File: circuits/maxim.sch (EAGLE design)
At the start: 5 parts, among them IC1 MAX662ACPA+

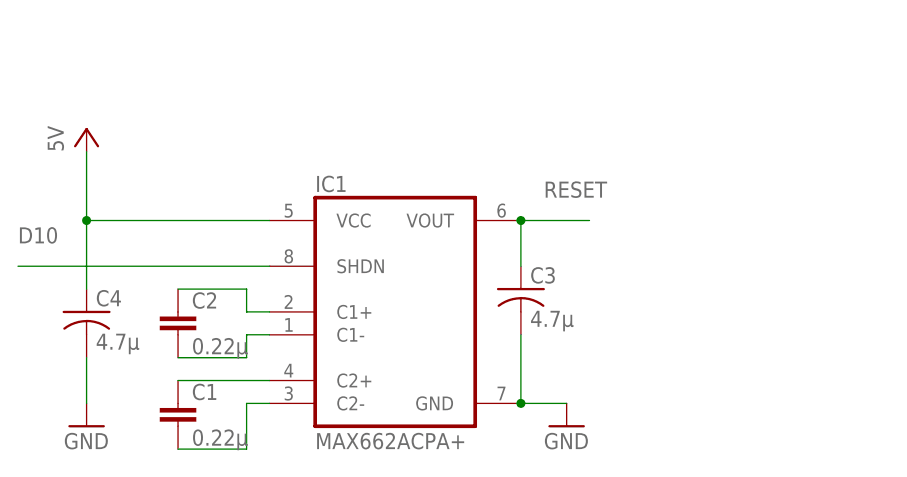
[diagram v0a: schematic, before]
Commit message: More documentation, started HVPP docs
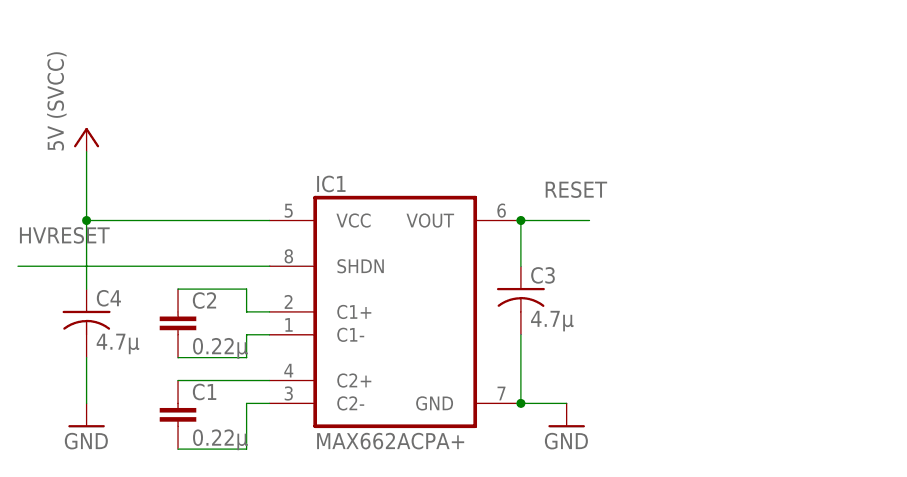
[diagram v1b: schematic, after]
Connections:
- net D10 renamed HVRESET
- net VCC renamed SVCC
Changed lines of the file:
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@@
 <part name="C2" library="rcl" deviceset="C-EU" device="025-024X044" value="0.22µ"/>
 <part name="GND1" library="supply1" deviceset="GND" device=""/>
-<part name="5V" library="supply1" deviceset="VCC" device="" value="5V"/>
+<part name="5V" library="supply1" deviceset="VCC" device="" value="5V (SVCC)"/>
 <part name="C3" library="rcl" deviceset="C-US" device="025-024X044" value="4.7µ"/>
 <part name="C4" library="rcl" deviceset="C-US" device="025-024X044" value="4.7µ"/>
@@
 </segment>
 </net>
-<net name="VCC" class="0">
+<net name="SVCC" class="0">
 <segment>
 <pinref part="IC1" gate="1" pin="VCC"/>
@@
 </segment>
 </net>
-<net name="D10" class="0">
+<net name="HVRESET" class="0">
 <segment>
 <pinref part="IC1" gate="1" pin="SHDN"/>

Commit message: Maxim circuit needs transistor anyway
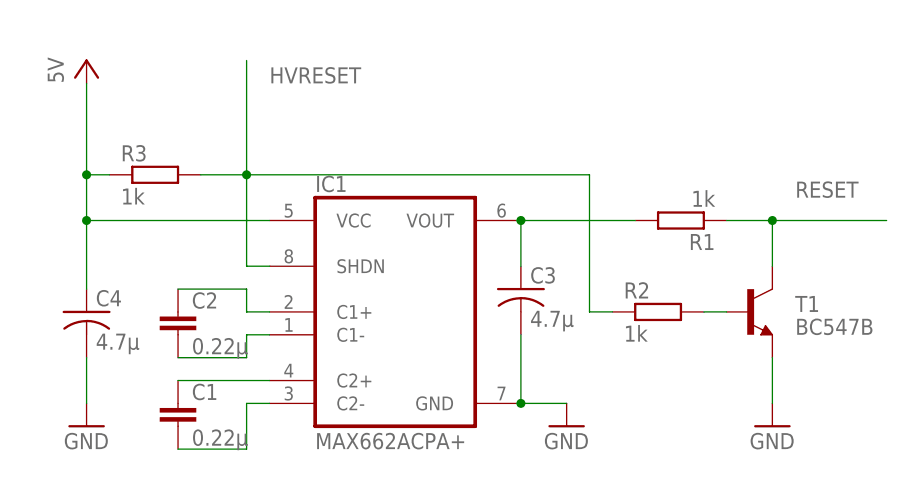
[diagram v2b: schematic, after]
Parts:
- added R1, R2, R3: 1k, eagle-ltspice:R
- added T1: BC547B, transistor:BC547
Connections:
- new net N$5: R2.2, T1.B
- new net VOUT: C3.1, IC1.VOUT, R1.2
- net GND: now also T1.E
- net HVRESET: now also R2.1, R3.2
- net RESET: now also R1.1, T1.C; no longer C3.1, IC1.VOUT
- net SVCC: now also R3.1
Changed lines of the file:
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@@
 <layer number="97" name="Info" color="7" fill="1" visible="yes" active="yes"/>
 <layer number="98" name="Guide" color="6" fill="1" visible="yes" active="yes"/>
+<layer number="99" name="SpiceOrder" color="5" fill="1" visible="yes" active="yes"/>
 </layers>
 <schematic xreflabel="%F%N/%S.%C%R" xrefpart="/%S.%C%R">
@@
 <part name="C2" library="rcl" deviceset="C-EU" device="025-024X044" value="0.22µ"/>
 <part name="GND1" library="supply1" deviceset="GND" device=""/>
-<part name="5V" library="supply1" deviceset="VCC" device="" value="5V (SVCC)"/>
+<part name="5V" library="supply1" deviceset="VCC" device="" value="5V"/>
 <part name="C3" library="rcl" deviceset="C-US" device="025-024X044" value="4.7µ"/>
 <part name="C4" library="rcl" deviceset="C-US" device="025-024X044" value="4.7µ"/>
 <part name="GND2" library="supply1" deviceset="GND" device=""/>
+<part name="T1" library="transistor" deviceset="BC547" device="" value="BC547B"/>
+<part name="GND3" library="supply1" deviceset="GND" device=""/>
+<part name="R1" library="eagle-ltspice" deviceset="R" device="" value="1k"/>
+<part name="R2" library="eagle-ltspice" deviceset="R" device="" value="1k"/>
+<part name="R3" library="eagle-ltspice" deviceset="R" device="" value="1k"/>
 </parts>
 <sheets>
@@
 <instance part="C2" gate="G$1" x="30.48" y="63.5"/>
 <instance part="GND1" gate="1" x="73.66" y="50.8"/>
-<instance part="5V" gate="VCC" x="20.32" y="83.82"/>
+<instance part="5V" gate="VCC" x="20.32" y="91.44"/>
 <instance part="C3" gate="G$1" x="68.58" y="66.04"/>
 <instance part="C4" gate="G$1" x="20.32" y="63.5"/>
 <instance part="GND2" gate="1" x="20.32" y="50.8"/>
+<instance part="T1" gate="G$1" x="93.98" y="63.5" smashed="yes">
+<attribute name="NAME" x="99.06" y="63.5" size="1.778" layer="95"/>
+<attribute name="VALUE" x="99.06" y="60.96" size="1.778" layer="96"/>
+</instance>
+<instance part="GND3" gate="1" x="96.52" y="50.8"/>
+<instance part="R1" gate="G$1" x="86.36" y="73.66" rot="R180"/>
+<instance part="R2" gate="G$1" x="83.82" y="63.5"/>
+<instance part="R3" gate="G$1" x="27.94" y="78.74"/>
 </instances>
 <busses>
@@
 <net name="RESET" class="0">
 <segment>
-<pinref part="IC1" gate="1" pin="VOUT"/>
-<wire x1="68.58" y1="73.66" x2="76.2" y2="73.66" width="0.1524" layer="91"/>
-<label x="71.12" y="76.2" size="1.778" layer="95"/>
-<pinref part="C3" gate="G$1" pin="1"/>
-<wire x1="68.58" y1="68.58" x2="68.58" y2="73.66" width="0.1524" layer="91"/>
-<junction x="68.58" y="73.66"/>
+<label x="99.06" y="76.2" size="1.778" layer="95"/>
+<pinref part="R1" gate="G$1" pin="1"/>
+<pinref part="T1" gate="G$1" pin="C"/>
+<wire x1="91.44" y1="73.66" x2="96.52" y2="73.66" width="0.1524" layer="91"/>
+<junction x="96.52" y="73.66"/>
+<wire x1="96.52" y1="73.66" x2="96.52" y2="68.58" width="0.1524" layer="91"/>
+<wire x1="96.52" y1="73.66" x2="109.22" y2="73.66" width="0.1524" layer="91"/>
 </segment>
 </net>
@@
 <pinref part="5V" gate="VCC" pin="VCC"/>
 <wire x1="40.64" y1="73.66" x2="20.32" y2="73.66" width="0.1524" layer="91"/>
-<wire x1="20.32" y1="73.66" x2="20.32" y2="81.28" width="0.1524" layer="91"/>
+<wire x1="20.32" y1="73.66" x2="20.32" y2="78.74" width="0.1524" layer="91"/>
 <pinref part="C4" gate="G$1" pin="1"/>
+<wire x1="20.32" y1="78.74" x2="20.32" y2="88.9" width="0.1524" layer="91"/>
 <wire x1="20.32" y1="73.66" x2="20.32" y2="66.04" width="0.1524" layer="91"/>
 <junction x="20.32" y="73.66"/>
+<pinref part="R3" gate="G$1" pin="1"/>
+<wire x1="20.32" y1="78.74" x2="22.86" y2="78.74" width="0.1524" layer="91"/>
+<junction x="20.32" y="78.74"/>
 </segment>
 </net>
@@
 <wire x1="20.32" y1="58.42" x2="20.32" y2="53.34" width="0.1524" layer="91"/>
 </segment>
+<segment>
+<pinref part="GND3" gate="1" pin="GND"/>
+<pinref part="T1" gate="G$1" pin="E"/>
+<wire x1="96.52" y1="53.34" x2="96.52" y2="58.42" width="0.1524" layer="91"/>
+</segment>
 </net>
 <net name="HVRESET" class="0">
 <segment>
 <pinref part="IC1" gate="1" pin="SHDN"/>
-<wire x1="40.64" y1="68.58" x2="12.7" y2="68.58" width="0.1524" layer="91"/>
-<label x="12.7" y="71.12" size="1.778" layer="95"/>
+<wire x1="40.64" y1="68.58" x2="38.1" y2="68.58" width="0.1524" layer="91"/>
+<wire x1="38.1" y1="68.58" x2="38.1" y2="78.74" width="0.1524" layer="91"/>
+<label x="40.64" y="88.9" size="1.778" layer="95"/>
+<junction x="38.1" y="78.74"/>
+<wire x1="38.1" y1="78.74" x2="38.1" y2="91.44" width="0.1524" layer="91"/>
+<wire x1="38.1" y1="78.74" x2="76.2" y2="78.74" width="0.1524" layer="91"/>
+<wire x1="76.2" y1="78.74" x2="76.2" y2="63.5" width="0.1524" layer="91"/>
+<pinref part="R2" gate="G$1" pin="1"/>
+<wire x1="78.74" y1="63.5" x2="76.2" y2="63.5" width="0.1524" layer="91"/>
+<pinref part="R3" gate="G$1" pin="2"/>
+<wire x1="33.02" y1="78.74" x2="38.1" y2="78.74" width="0.1524" layer="91"/>
 </segment>
 </net>
+<net name="N$5" class="0">
+<segment>
+<pinref part="T1" gate="G$1" pin="B"/>
+<pinref part="R2" gate="G$1" pin="2"/>
+<wire x1="88.9" y1="63.5" x2="91.44" y2="63.5" width="0.1524" layer="91"/>
+</segment>
+</net>
+<net name="VOUT" class="0">
+<segment>
+<pinref part="IC1" gate="1" pin="VOUT"/>
+<pinref part="C3" gate="G$1" pin="1"/>
+<wire x1="68.58" y1="68.58" x2="68.58" y2="73.66" width="0.1524" layer="91"/>
+<pinref part="R1" gate="G$1" pin="2"/>
+<wire x1="68.58" y1="73.66" x2="81.28" y2="73.66" width="0.1524" layer="91"/>
+<junction x="68.58" y="73.66"/>
+</segment>
+</net>

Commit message: Final HV documentation tweaks before release
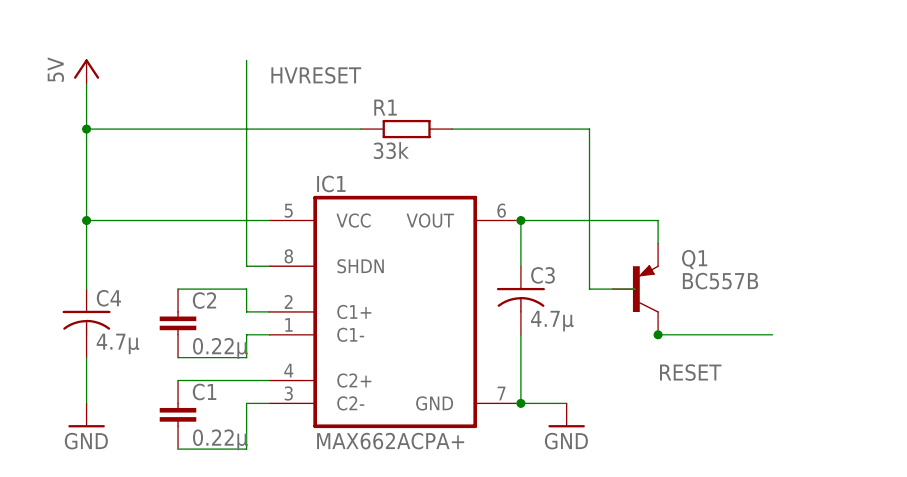
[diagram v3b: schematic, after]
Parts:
- removed R2, R3: 1k, eagle-ltspice:R
- removed T1: BC547B, transistor:BC547
- added Q1: BC557B, transistor-pnp:BC557B
- R1: value 1k -> 33k
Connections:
- removed net N$5: R2.2, T1.B
- new net N$7: R1.2
- net GND: no longer T1.E
- net HVRESET: no longer R2.1, R3.2
- net RESET: now also Q1.C; no longer R1.1, T1.C
- net SVCC: now also R1.1; no longer R3.1
- net VOUT: now also Q1.E; no longer R1.2
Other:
- moved on the sheet: R1
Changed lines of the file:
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@@
 <part name="C4" library="rcl" deviceset="C-US" device="025-024X044" value="4.7µ"/>
 <part name="GND2" library="supply1" deviceset="GND" device=""/>
-<part name="T1" library="transistor" deviceset="BC547" device="" value="BC547B"/>
-<part name="GND3" library="supply1" deviceset="GND" device=""/>
-<part name="R1" library="eagle-ltspice" deviceset="R" device="" value="1k"/>
-<part name="R2" library="eagle-ltspice" deviceset="R" device="" value="1k"/>
-<part name="R3" library="eagle-ltspice" deviceset="R" device="" value="1k"/>
+<part name="Q1" library="transistor-pnp" deviceset="BC557*" device="" technology="B"/>
+<part name="R1" library="eagle-ltspice" deviceset="R" device="" value="33k"/>
 </parts>
 <sheets>
@@
 <instance part="C4" gate="G$1" x="20.32" y="63.5"/>
 <instance part="GND2" gate="1" x="20.32" y="50.8"/>
-<instance part="T1" gate="G$1" x="93.98" y="63.5" smashed="yes">
-<attribute name="NAME" x="99.06" y="63.5" size="1.778" layer="95"/>
-<attribute name="VALUE" x="99.06" y="60.96" size="1.778" layer="96"/>
+<instance part="Q1" gate="G$1" x="81.28" y="66.04" smashed="yes">
+<attribute name="NAME" x="86.36" y="68.58" size="1.778" layer="95"/>
+<attribute name="VALUE" x="86.36" y="66.04" size="1.778" layer="96"/>
 </instance>
-<instance part="GND3" gate="1" x="96.52" y="50.8"/>
-<instance part="R1" gate="G$1" x="86.36" y="73.66" rot="R180"/>
-<instance part="R2" gate="G$1" x="83.82" y="63.5"/>
-<instance part="R3" gate="G$1" x="27.94" y="78.74"/>
+<instance part="R1" gate="G$1" x="55.88" y="83.82"/>
 </instances>
 <busses>
@@
 <net name="RESET" class="0">
 <segment>
-<label x="99.06" y="76.2" size="1.778" layer="95"/>
-<pinref part="R1" gate="G$1" pin="1"/>
-<pinref part="T1" gate="G$1" pin="C"/>
-<wire x1="91.44" y1="73.66" x2="96.52" y2="73.66" width="0.1524" layer="91"/>
-<junction x="96.52" y="73.66"/>
-<wire x1="96.52" y1="73.66" x2="96.52" y2="68.58" width="0.1524" layer="91"/>
-<wire x1="96.52" y1="73.66" x2="109.22" y2="73.66" width="0.1524" layer="91"/>
+<label x="83.82" y="55.88" size="1.778" layer="95"/>
+<wire x1="83.82" y1="60.96" x2="96.52" y2="60.96" width="0.1524" layer="91"/>
+<pinref part="Q1" gate="G$1" pin="C"/>
+<junction x="83.82" y="60.96"/>
 </segment>
 </net>
@@
 <pinref part="5V" gate="VCC" pin="VCC"/>
 <wire x1="40.64" y1="73.66" x2="20.32" y2="73.66" width="0.1524" layer="91"/>
-<wire x1="20.32" y1="73.66" x2="20.32" y2="78.74" width="0.1524" layer="91"/>
 <pinref part="C4" gate="G$1" pin="1"/>
-<wire x1="20.32" y1="78.74" x2="20.32" y2="88.9" width="0.1524" layer="91"/>
+<wire x1="20.32" y1="73.66" x2="20.32" y2="83.82" width="0.1524" layer="91"/>
+<wire x1="20.32" y1="83.82" x2="20.32" y2="88.9" width="0.1524" layer="91"/>
 <wire x1="20.32" y1="73.66" x2="20.32" y2="66.04" width="0.1524" layer="91"/>
 <junction x="20.32" y="73.66"/>
-<pinref part="R3" gate="G$1" pin="1"/>
-<wire x1="20.32" y1="78.74" x2="22.86" y2="78.74" width="0.1524" layer="91"/>
-<junction x="20.32" y="78.74"/>
+<wire x1="50.8" y1="83.82" x2="20.32" y2="83.82" width="0.1524" layer="91"/>
+<junction x="20.32" y="83.82"/>
+<pinref part="R1" gate="G$1" pin="1"/>
 </segment>
 </net>
@@
 <wire x1="20.32" y1="58.42" x2="20.32" y2="53.34" width="0.1524" layer="91"/>
 </segment>
-<segment>
-<pinref part="GND3" gate="1" pin="GND"/>
-<pinref part="T1" gate="G$1" pin="E"/>
-<wire x1="96.52" y1="53.34" x2="96.52" y2="58.42" width="0.1524" layer="91"/>
-</segment>
 </net>
 <net name="HVRESET" class="0">
@@
 <pinref part="IC1" gate="1" pin="SHDN"/>
 <wire x1="40.64" y1="68.58" x2="38.1" y2="68.58" width="0.1524" layer="91"/>
-<wire x1="38.1" y1="68.58" x2="38.1" y2="78.74" width="0.1524" layer="91"/>
 <label x="40.64" y="88.9" size="1.778" layer="95"/>
-<junction x="38.1" y="78.74"/>
-<wire x1="38.1" y1="78.74" x2="38.1" y2="91.44" width="0.1524" layer="91"/>
-<wire x1="38.1" y1="78.74" x2="76.2" y2="78.74" width="0.1524" layer="91"/>
-<wire x1="76.2" y1="78.74" x2="76.2" y2="63.5" width="0.1524" layer="91"/>
-<pinref part="R2" gate="G$1" pin="1"/>
-<wire x1="78.74" y1="63.5" x2="76.2" y2="63.5" width="0.1524" layer="91"/>
-<pinref part="R3" gate="G$1" pin="2"/>
-<wire x1="33.02" y1="78.74" x2="38.1" y2="78.74" width="0.1524" layer="91"/>
-</segment>
-</net>
-<net name="N$5" class="0">
-<segment>
-<pinref part="T1" gate="G$1" pin="B"/>
-<pinref part="R2" gate="G$1" pin="2"/>
-<wire x1="88.9" y1="63.5" x2="91.44" y2="63.5" width="0.1524" layer="91"/>
+<wire x1="38.1" y1="68.58" x2="38.1" y2="91.44" width="0.1524" layer="91"/>
 </segment>
 </net>
@@
 <pinref part="C3" gate="G$1" pin="1"/>
 <wire x1="68.58" y1="68.58" x2="68.58" y2="73.66" width="0.1524" layer="91"/>
-<pinref part="R1" gate="G$1" pin="2"/>
-<wire x1="68.58" y1="73.66" x2="81.28" y2="73.66" width="0.1524" layer="91"/>
+<pinref part="Q1" gate="G$1" pin="E"/>
+<wire x1="83.82" y1="71.12" x2="83.82" y2="73.66" width="0.1524" layer="91"/>
+<wire x1="83.82" y1="73.66" x2="68.58" y2="73.66" width="0.1524" layer="91"/>
 <junction x="68.58" y="73.66"/>
 </segment>
 </net>
+<net name="N$7" class="0">
+<segment>
+<pinref part="R1" gate="G$1" pin="2"/>
+<wire x1="60.96" y1="83.82" x2="76.2" y2="83.82" width="0.1524" layer="91"/>
+<wire x1="81.28" y1="66.04" x2="76.2" y2="66.04" width="0.1524" layer="91"/>
+<wire x1="76.2" y1="66.04" x2="76.2" y2="83.82" width="0.1524" layer="91"/>
+</segment>
+</net>
